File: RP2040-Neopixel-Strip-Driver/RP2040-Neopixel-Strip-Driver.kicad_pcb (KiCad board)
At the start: 4 copper layers, 10.2 x 47 mm, 48 parts, among them J201 TYPE-C-31-M-12, J202 Conn_01x03, J203 NeopixelStrip, J204 5V, J205 TO BE DECIDED, J206 GND, SW202 ~{USB_BOOT}, U201 XC6206P332MR, U202 RP2040, U205 W25Q128JVPIQ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

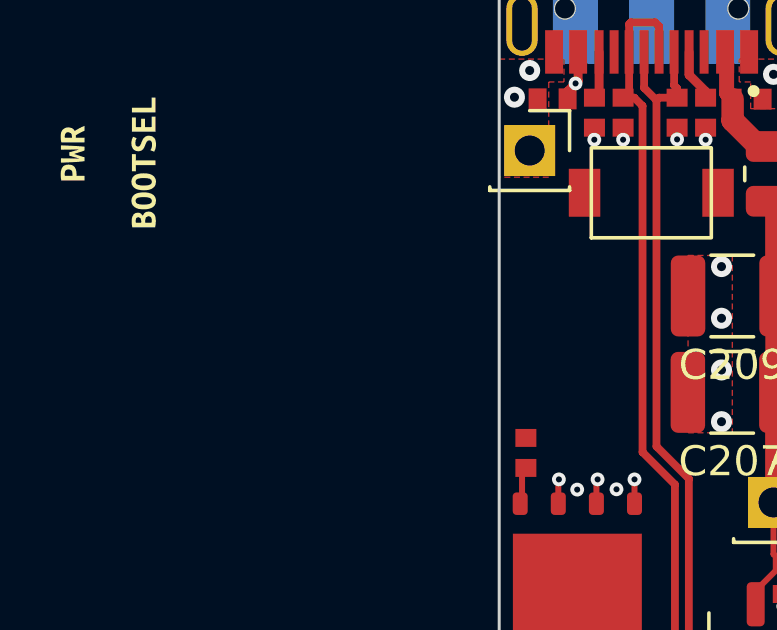
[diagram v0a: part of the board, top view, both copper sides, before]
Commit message: Added level shifter
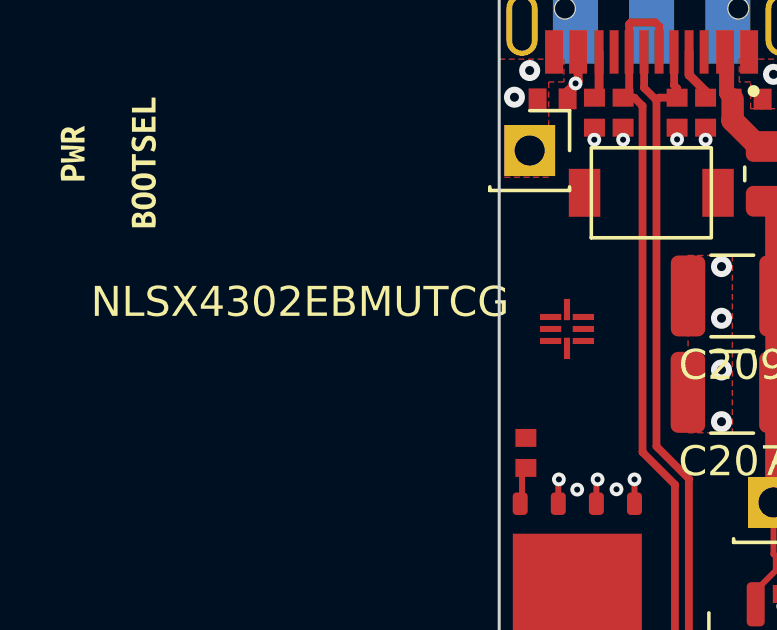
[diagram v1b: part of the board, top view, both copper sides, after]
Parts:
- added U101: NLSX4302EBMUTCG, NLSX4302EBMUTCG:NLSX4302EBMUTCG, F.Cu at (144.1, 43.6)

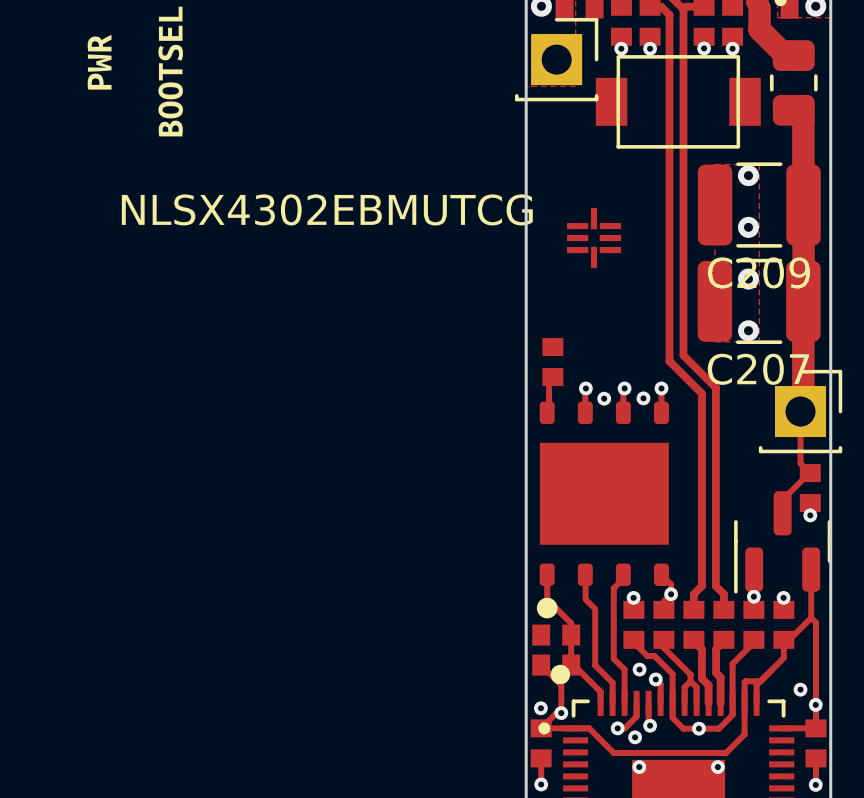
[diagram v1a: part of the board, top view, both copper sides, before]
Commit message: Added model for level shifter and added 3Daccelerometer+3Dgyroscope
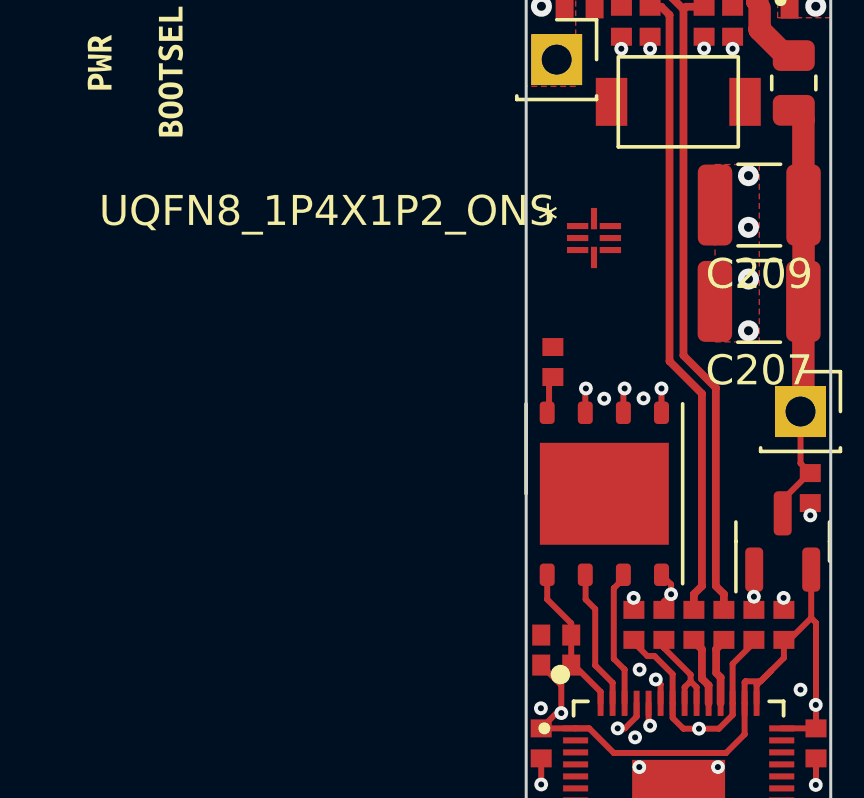
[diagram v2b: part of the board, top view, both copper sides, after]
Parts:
- U101: value NLSX4302EBMUTCG -> UQFN8_1P4X1P2_ONS

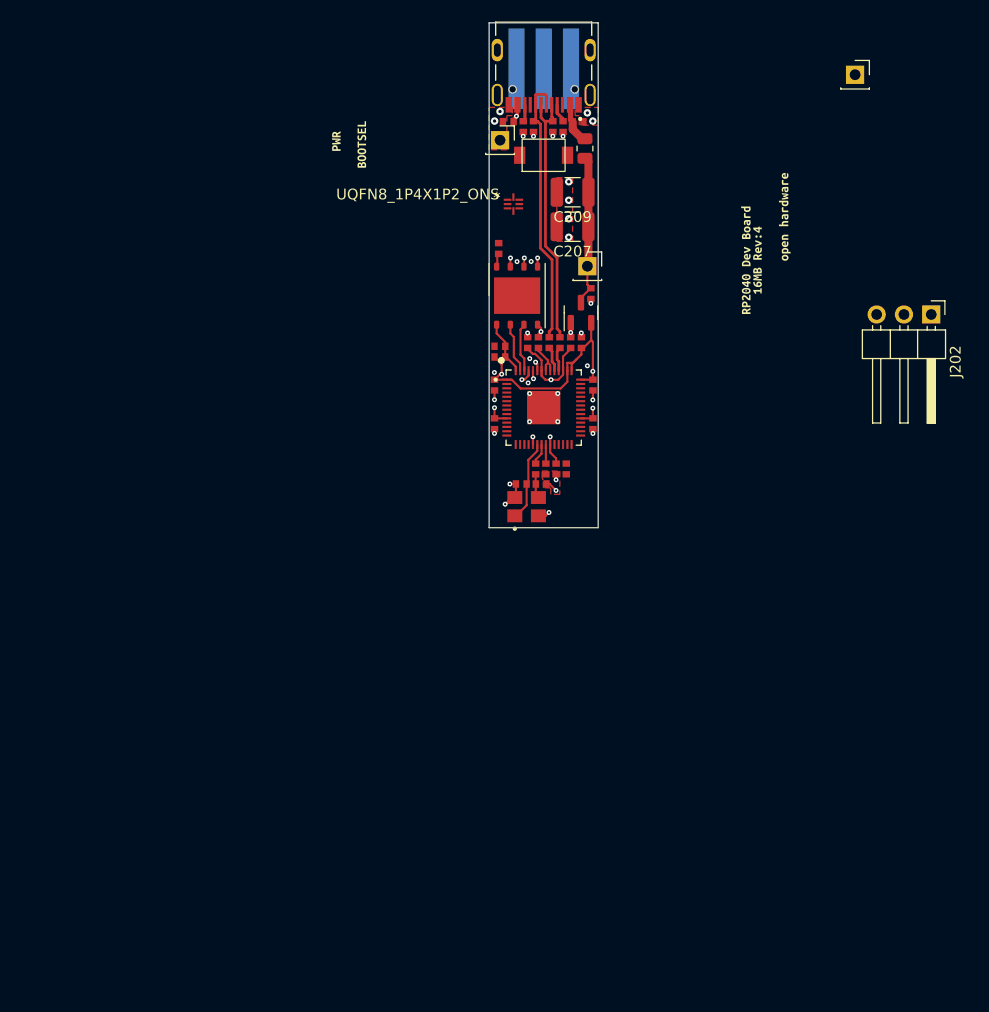
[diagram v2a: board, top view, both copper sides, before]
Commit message: Project Expansion/Pivot - This is now a very involved cosplay prop tool.
Looking to incorporate a lot:
3D Gyro + 3D Accelerometer
Neopixel Driver
Speaker Driver
Microphone
SD Card Connector
Battery
Etc.
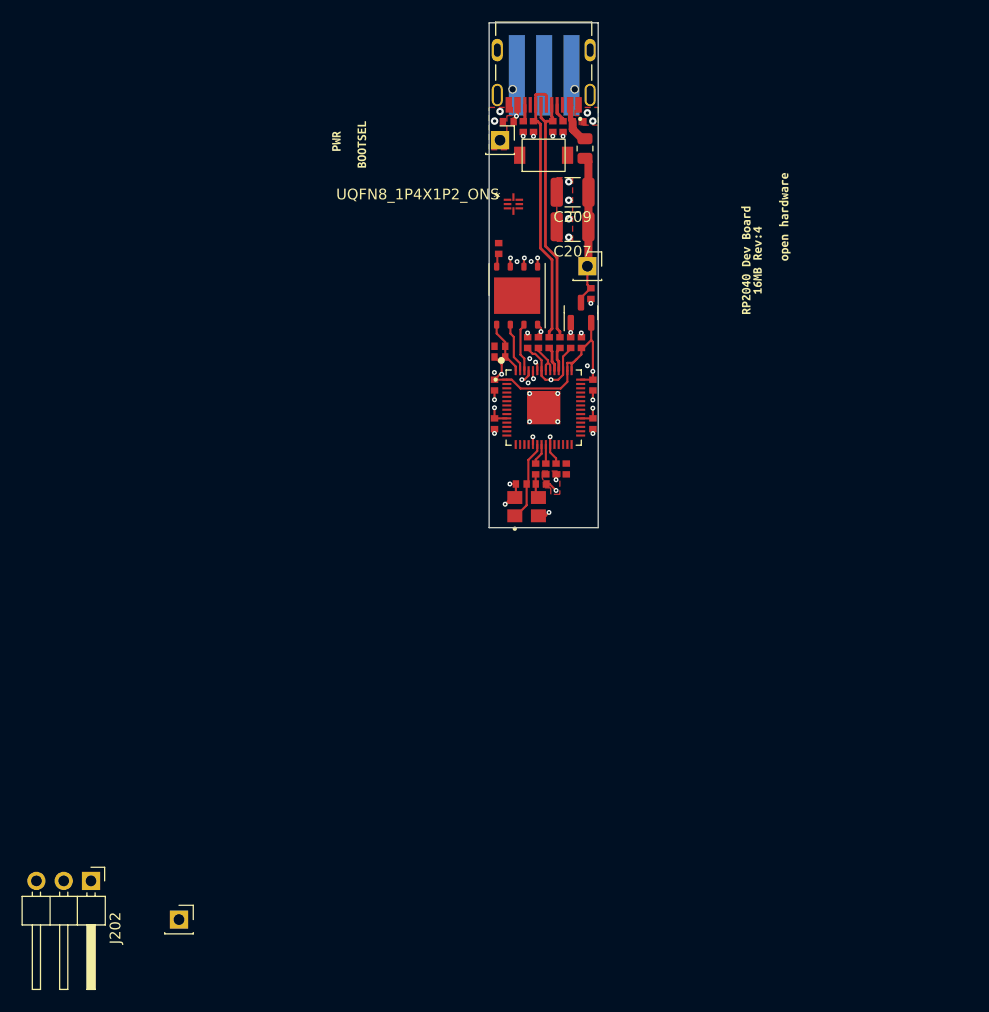
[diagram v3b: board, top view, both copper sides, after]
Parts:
- moved J205 100.7 mm to (113.0, 110.2)
- moved J202 94.3 mm to (104.8, 106.6)
- moved J203 0.61 mm to (146.9, 31.6)
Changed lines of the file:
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@@
   )
   (footprint "Connector_PinHeader_2.54mm:PinHeader_1x03_P2.54mm_Horizontal" (layer "F.Cu")
-    (at 182.98 53.906 -90)
+    (at 104.775 106.625 -90)
     (descr "Through hole angled pin header, 1x03, 2.54mm pitch, 6mm pin length, single row")
     (tags "Through hole angled pin header THT 1x03 2.54mm single row")
@@
     (pad "1" thru_hole rect locked (at 0 0) (size 1.7 1.7) (drill 1) (layers *.Cu *.Mask)
       (net 1 "GND") (pinfunction "Pin_1") (pintype "passive"))
-    (model "${KICAD6_3DMODEL_DIR}/Connector_PinSocket_2.54mm.3dshapes/PinSocket_1x01_P2.54mm_Vertical.wrl"
+    (model "${KICAD6_3DMODEL_DIR}/Connector_PinSocket_2.54mm.3dshapes/PinSocket_1x01_P2.54mm_Vertical.wrl" hide
       (offset (xyz 0 0 0))
       (scale (xyz 1 1 1))
@@
     (pad "1" thru_hole rect locked (at 0 0) (size 1.7 1.7) (drill 1) (layers *.Cu *.Mask)
       (net 57 "VBUS") (pinfunction "Pin_1") (pintype "passive"))
-    (model "${KICAD6_3DMODEL_DIR}/Connector_PinSocket_2.54mm.3dshapes/PinSocket_1x01_P2.54mm_Vertical.wrl"
+    (model "${KICAD6_3DMODEL_DIR}/Connector_PinSocket_2.54mm.3dshapes/PinSocket_1x01_P2.54mm_Vertical.wrl" hide
       (offset (xyz 0 0 0))
       (scale (xyz 1 1 1))
@@
   )
   (footprint "Connector_PinSocket_2.54mm:PinSocket_1x01_P2.54mm_Vertical" (layer "F.Cu")
-    (at 175.89 31.59)
+    (at 112.965 110.225)
     (descr "Through hole straight socket strip, 1x01, 2.54mm pitch, single row (from Kicad 4.0.7), script generated")
     (tags "Through hole socket strip THT 1x01 2.54mm single row")
@@
   )
   (footprint "Breadstick Footprints:NeopixelStrip" (layer "B.Cu")
-    (at 146.91 31.04 180)
+    (at 146.95 31.65 180)
     (property "Sheetfile" "RP2040.kicad_sch")
     (property "Sheetname" "RP2040")
